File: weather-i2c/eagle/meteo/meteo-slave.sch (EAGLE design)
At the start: 38 parts, among them CON1 SPI, IC1 MCP1703CB, J2 RJ12RIGHTANGLE-I2C, J3 RJ12RIGHTANGLE-I2C, U1 ATMEGA328P_TQFP, X1 8MHz, X2 1503_09, X3 1503_09

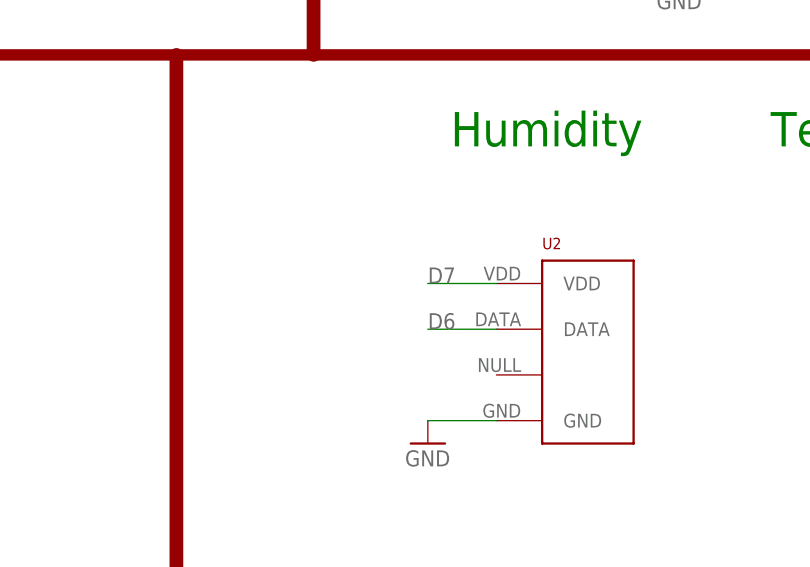
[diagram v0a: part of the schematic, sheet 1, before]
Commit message: weather-slave: add 4.7k for humidity sensor
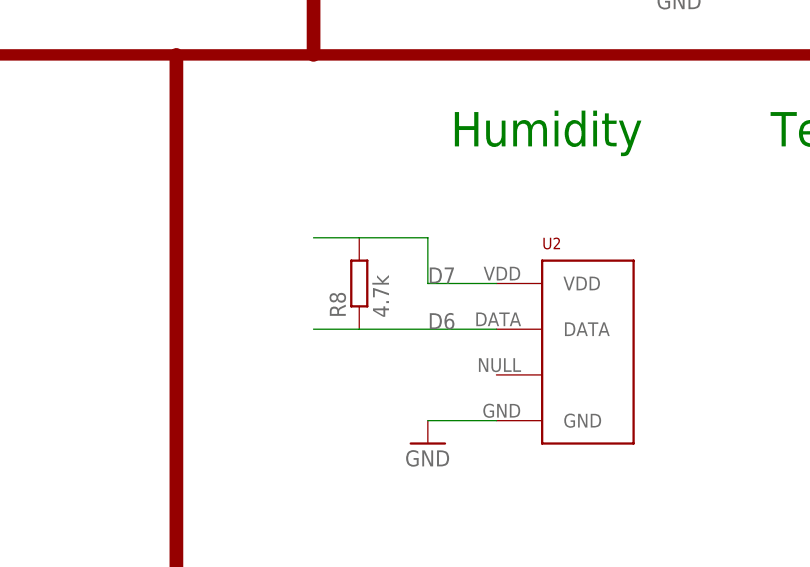
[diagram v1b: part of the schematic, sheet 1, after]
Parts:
- added R8: 4.7k, resistor:R-EU_R0805
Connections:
- net D6: now also R8.1
- net D7: now also R8.2
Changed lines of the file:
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@@
 </part>
 <part name="GND7" library="supply1" library_urn="urn:adsk.eagle:library:371" deviceset="GND" device=""/>
+<part name="R8" library="resistor" library_urn="urn:adsk.eagle:library:348" deviceset="R-EU_" device="R0805" value="4.7k"/>
 </parts>
 <sheets>
@@
 <attribute name="VALUE" x="254.635" y="140.335" size="1.27" layer="96"/>
 </instance>
+<instance part="R8" gate="G$1" x="93.98" y="35.56" rot="R90"/>
 </instances>
 <busses>
@@
 <segment>
 <pinref part="U2" gate="G$1" pin="DATA"/>
-<wire x1="109.22" y1="30.48" x2="101.6" y2="30.48" width="0.1524" layer="91"/>
 <label x="101.6" y="30.48" size="1.778" layer="95"/>
+<pinref part="R8" gate="G$1" pin="1"/>
+<wire x1="109.22" y1="30.48" x2="93.98" y2="30.48" width="0.1524" layer="91"/>
+<wire x1="93.98" y1="30.48" x2="88.9" y2="30.48" width="0.1524" layer="91"/>
 </segment>
 </net>
@@
 <wire x1="101.6" y1="35.56" x2="109.22" y2="35.56" width="0.1524" layer="91"/>
 <label x="101.6" y="35.56" size="1.778" layer="95"/>
-</segment>
-</net>
+<wire x1="101.6" y1="35.56" x2="101.6" y2="40.64" width="0.1524" layer="91"/>
+<pinref part="R8" gate="G$1" pin="2"/>
+<wire x1="101.6" y1="40.64" x2="93.98" y2="40.64" width="0.1524" layer="91"/>
+<wire x1="93.98" y1="40.64" x2="88.9" y2="40.64" width="0.1524" layer="91"/>
+</segment>
+</net>

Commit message: weather-i2c: cleanup v1.1
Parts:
- added R10, R11: 4.7k, resistor:R-EU_R0805
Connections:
- net D8: now also R10.1
- net D9: now also R11.1
- net VCC: now also R10.2, R11.2
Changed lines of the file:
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@@
 <part name="GND14" library="supply1" library_urn="urn:adsk.eagle:library:371" deviceset="GND" device=""/>
 <part name="C2" library="rcl" library_urn="urn:adsk.eagle:library:334" deviceset="C-EU" device="C0805K" package3d_urn="urn:adsk.eagle:package:23681/2" value="10u">
+<spice>
+<pinmapping spiceprefix="C">
+<pinmap gate="G$1" pin="1" pinorder="1"/>
+<pinmap gate="G$1" pin="2" pinorder="2"/>
+</pinmapping>
+</spice>
 <attribute name="ELECROW" value="C15850"/>
 <attribute name="LCSC" value="C15850"/>
@@
 <part name="GND19" library="supply1" library_urn="urn:adsk.eagle:library:371" deviceset="GND" device=""/>
 <part name="C3" library="rcl" library_urn="urn:adsk.eagle:library:334" deviceset="C-EU" device="C0805K" package3d_urn="urn:adsk.eagle:package:23681/2" value="10u">
+<spice>
+<pinmapping spiceprefix="C">
+<pinmap gate="G$1" pin="1" pinorder="1"/>
+<pinmap gate="G$1" pin="2" pinorder="2"/>
+</pinmapping>
+</spice>
 <attribute name="ELECROW" value="C15850"/>
 <attribute name="LCSC" value="C15850"/>
@@
 <part name="P+1" library="supply1" library_urn="urn:adsk.eagle:library:371" deviceset="VCC" device=""/>
 <part name="C4" library="rcl" library_urn="urn:adsk.eagle:library:334" deviceset="C-EU" device="C0805K" package3d_urn="urn:adsk.eagle:package:23681/2" value="100nF">
+<spice>
+<pinmapping spiceprefix="C">
+<pinmap gate="G$1" pin="1" pinorder="1"/>
+<pinmap gate="G$1" pin="2" pinorder="2"/>
+</pinmapping>
+</spice>
 <attribute name="ELECROW" value="C49678"/>
 <attribute name="LCSC" value="C49678"/>
@@
 </part>
 <part name="C6" library="rcl" library_urn="urn:adsk.eagle:library:334" deviceset="C-EU" device="C0805K" package3d_urn="urn:adsk.eagle:package:23681/2" value="100nF">
+<spice>
+<pinmapping spiceprefix="C">
+<pinmap gate="G$1" pin="1" pinorder="1"/>
+<pinmap gate="G$1" pin="2" pinorder="2"/>
+</pinmapping>
+</spice>
 <attribute name="ELECROW" value="C49678"/>
 <attribute name="LCSC" value="C49678"/>
@@
 </part>
 <part name="C5" library="rcl" library_urn="urn:adsk.eagle:library:334" deviceset="C-EU" device="C0805K" package3d_urn="urn:adsk.eagle:package:23681/2" value="100nF">
+<spice>
+<pinmapping spiceprefix="C">
+<pinmap gate="G$1" pin="1" pinorder="1"/>
+<pinmap gate="G$1" pin="2" pinorder="2"/>
+</pinmapping>
+</spice>
 <attribute name="ELECROW" value="C49678"/>
 <attribute name="LCSC" value="C49678"/>
@@
 <part name="GND13" library="SparkFun" deviceset="GND" device=""/>
 <part name="C7" library="rcl" library_urn="urn:adsk.eagle:library:334" deviceset="C-EU" device="C0805K" package3d_urn="urn:adsk.eagle:package:23681/2" value="18pF">
+<spice>
+<pinmapping spiceprefix="C">
+<pinmap gate="G$1" pin="1" pinorder="1"/>
+<pinmap gate="G$1" pin="2" pinorder="2"/>
+</pinmapping>
+</spice>
 <attribute name="ELECROW" value="C1797"/>
 <attribute name="LCSC" value="C1797"/>
@@
 </part>
 <part name="C8" library="rcl" library_urn="urn:adsk.eagle:library:334" deviceset="C-EU" device="C0805K" package3d_urn="urn:adsk.eagle:package:23681/2" value="18pF">
+<spice>
+<pinmapping spiceprefix="C">
+<pinmap gate="G$1" pin="1" pinorder="1"/>
+<pinmap gate="G$1" pin="2" pinorder="2"/>
+</pinmapping>
+</spice>
 <attribute name="ELECROW" value="C1797"/>
 <attribute name="LCSC" value="C1797"/>
@@
 </part>
 <part name="R1" library="SparkFun" deviceset="PHOTOCELL" device="PTH"/>
-<part name="R2" library="resistor" library_urn="urn:adsk.eagle:library:348" deviceset="R-EU_" device="R0805" value="10k"/>
+<part name="R2" library="resistor" library_urn="urn:adsk.eagle:library:348" deviceset="R-EU_" device="R0805" package3d_urn="urn:adsk.eagle:package:26059/1" value="10k"/>
 <part name="GND2" library="supply1" library_urn="urn:adsk.eagle:library:371" deviceset="GND" device=""/>
 <part name="U$1" library="Ava" deviceset="DS1820" device="TO92"/>
-<part name="R4" library="resistor" library_urn="urn:adsk.eagle:library:348" deviceset="R-EU_" device="R0805" value="4.7k"/>
+<part name="R4" library="resistor" library_urn="urn:adsk.eagle:library:348" deviceset="R-EU_" device="R0805" package3d_urn="urn:adsk.eagle:package:26059/1" value="4.7k"/>
 <part name="GND4" library="supply1" library_urn="urn:adsk.eagle:library:371" deviceset="GND" device=""/>
 <part name="U2" library="RHT03_DHT-22_AM2302" deviceset="RHT03_DHT-22_AM2302" device=""/>
@@
 <part name="R21" library="resistor" deviceset="R-EU_" device="R0805" value="4.7k"/>
 <part name="R9" library="rcl" deviceset="R-EU_" device="R0805" value="1K"/>
-<part name="X2" library="con-lumberg" deviceset="1503_09" device=""/>
+<part name="X2" library="con-lumberg" library_urn="urn:adsk.eagle:library:163" deviceset="1503_09" device="" package3d_urn="urn:adsk.eagle:package:8555/1"/>
 <part name="R5" library="rcl" deviceset="R-EU_" device="R0805" value="100"/>
 <part name="GND1" library="supply1" deviceset="GND" device=""/>
 <part name="R22" library="resistor" deviceset="R-EU_" device="R0805" value="4.7k"/>
 <part name="R6" library="rcl" deviceset="R-EU_" device="R0805" value="1K"/>
-<part name="X3" library="con-lumberg" deviceset="1503_09" device=""/>
+<part name="X3" library="con-lumberg" library_urn="urn:adsk.eagle:library:163" deviceset="1503_09" device="" package3d_urn="urn:adsk.eagle:package:8555/1"/>
 <part name="R7" library="rcl" deviceset="R-EU_" device="R0805" value="100"/>
 <part name="R18" library="rcl" deviceset="R-EU_" device="R0805" value="1M">
@@
 </part>
 <part name="C11" library="rcl" library_urn="urn:adsk.eagle:library:334" deviceset="C-EU" device="C0805K" package3d_urn="urn:adsk.eagle:package:23681/2" value="100nF">
+<spice>
+<pinmapping spiceprefix="C">
+<pinmap gate="G$1" pin="1" pinorder="1"/>
+<pinmap gate="G$1" pin="2" pinorder="2"/>
+</pinmapping>
+</spice>
 <attribute name="ELECROW" value="C49678"/>
 <attribute name="LCSC" value="C49678"/>
@@
 </part>
 <part name="GND7" library="supply1" library_urn="urn:adsk.eagle:library:371" deviceset="GND" device=""/>
-<part name="R8" library="resistor" library_urn="urn:adsk.eagle:library:348" deviceset="R-EU_" device="R0805" value="4.7k"/>
+<part name="R8" library="resistor" library_urn="urn:adsk.eagle:library:348" deviceset="R-EU_" device="R0805" package3d_urn="urn:adsk.eagle:package:26059/1" value="4.7k"/>
+<part name="R10" library="resistor" library_urn="urn:adsk.eagle:library:348" deviceset="R-EU_" device="R0805" package3d_urn="urn:adsk.eagle:package:26059/1" value="4.7k"/>
+<part name="R11" library="resistor" library_urn="urn:adsk.eagle:library:348" deviceset="R-EU_" device="R0805" package3d_urn="urn:adsk.eagle:package:26059/1" value="4.7k"/>
+<part name="P+4" library="SparkFun" deviceset="3.3V" device="" value="VCC"/>
 </parts>
 <sheets>
@@
 </instance>
 <instance part="R8" gate="G$1" x="93.98" y="35.56" rot="R90"/>
+<instance part="R10" gate="G$1" x="193.04" y="91.44" rot="R90"/>
+<instance part="R11" gate="G$1" x="203.2" y="88.9" rot="R90"/>
+<instance part="P+4" gate="G$1" x="198.12" y="99.06"/>
 </instances>
 <busses>
@@
 <label x="5.08" y="38.1" size="1.778" layer="95"/>
 </segment>
+<segment>
+<pinref part="R10" gate="G$1" pin="2"/>
+<wire x1="193.04" y1="96.52" x2="193.04" y2="99.06" width="0.1524" layer="91"/>
+<wire x1="193.04" y1="99.06" x2="198.12" y2="99.06" width="0.1524" layer="91"/>
+<pinref part="R11" gate="G$1" pin="2"/>
+<wire x1="198.12" y1="99.06" x2="203.2" y2="99.06" width="0.1524" layer="91"/>
+<wire x1="203.2" y1="99.06" x2="203.2" y2="93.98" width="0.1524" layer="91"/>
+<pinref part="P+4" gate="G$1" pin="3.3V"/>
+<junction x="198.12" y="99.06"/>
+<label x="198.12" y="96.52" size="1.778" layer="95"/>
+</segment>
 </net>
 <net name="TX" class="0">
@@
 <label x="182.88" y="83.82" size="1.27" layer="95"/>
 <pinref part="U1" gate="U1" pin="PB1(OC1A)"/>
+<pinref part="R11" gate="G$1" pin="1"/>
+<wire x1="203.2" y1="83.82" x2="182.88" y2="83.82" width="0.1524" layer="91"/>
 </segment>
 <segment>
@@
 <label x="182.88" y="86.36" size="1.27" layer="95"/>
 <pinref part="U1" gate="U1" pin="PB0(ICP)"/>
+<pinref part="R10" gate="G$1" pin="1"/>
+<wire x1="182.88" y1="86.36" x2="193.04" y2="86.36" width="0.1524" layer="91"/>
 </segment>
 <segment>
@@
 packages will not be understood (or retained) with this version.
 </note>
+<note version="8.4" severity="warning">
+Since Version 8.4, EAGLE supports properties for SPICE simulation.
+Probes in schematics and SPICE mapping objects found in parts and library devices
+will not be understood with this version. Update EAGLE to the latest version
+for full support of SPICE simulation.
+</note>
 </compatibility>
